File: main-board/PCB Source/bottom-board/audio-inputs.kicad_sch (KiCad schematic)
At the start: 86 parts, among them P10 JACK_TRS_6PINS, P9 JACK_TRS_6PINS, Q1 2N7002, Q2 2N7002, Q3 MMBFJ211, Q4 MMBFJ211, Q5 MMBFJ211, Q6 MMBFJ211, Q7 2N7002, Q8 2N7002, U14 LM833DR2G, U5 LM4562

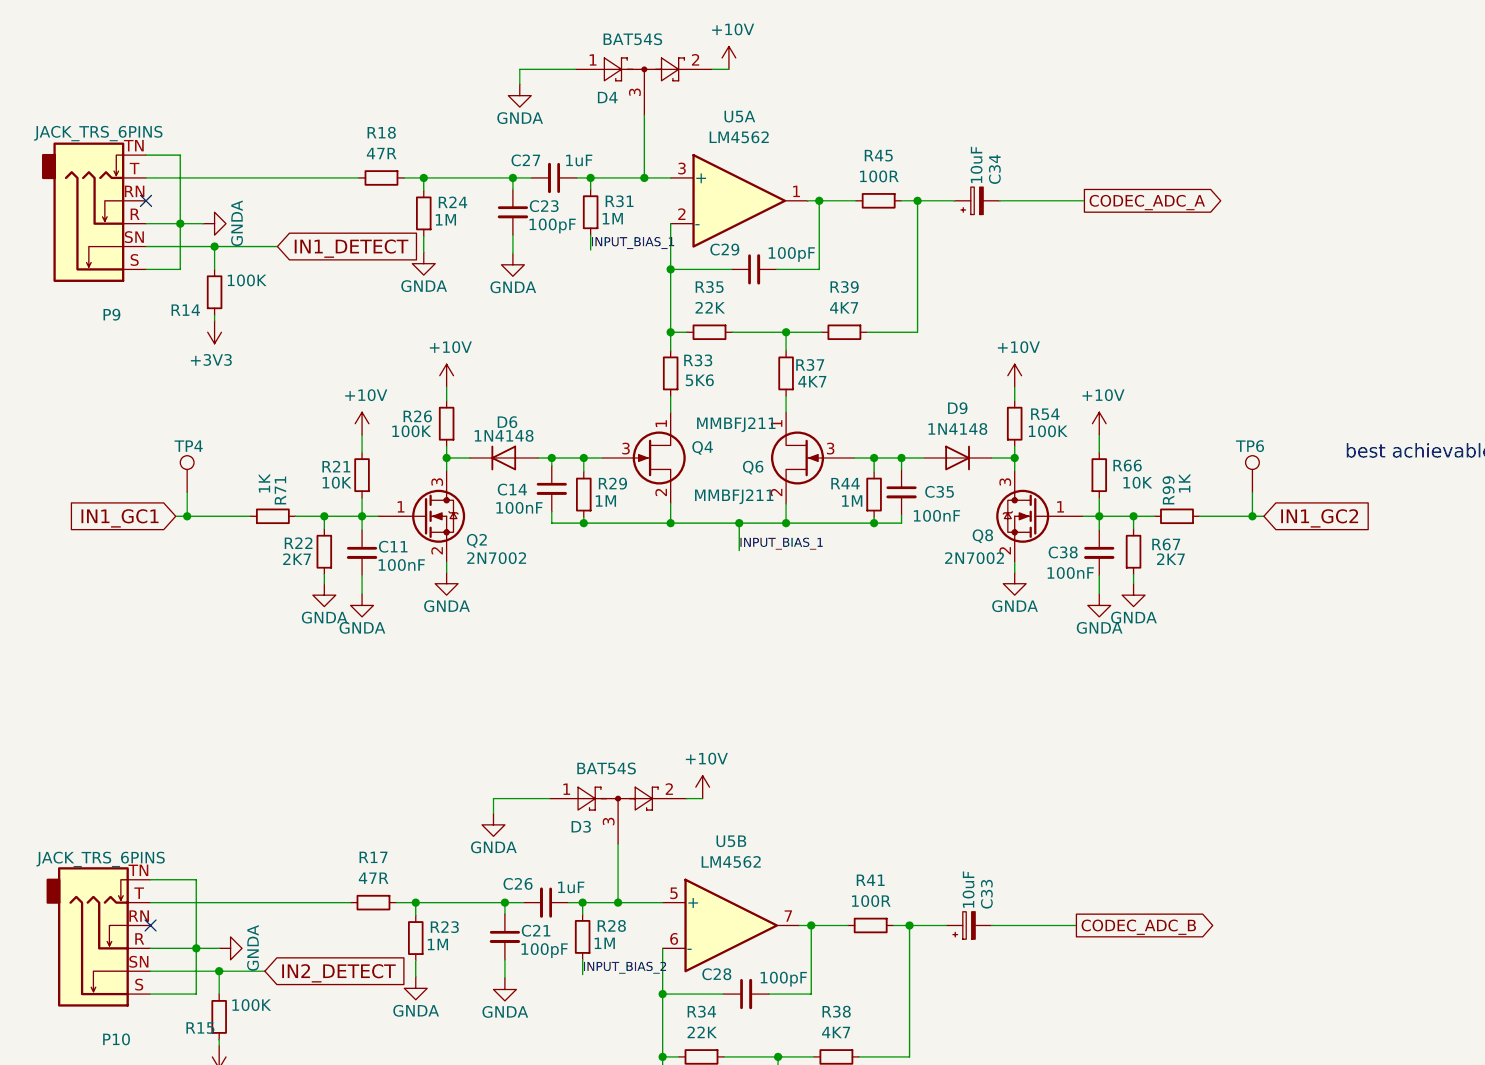
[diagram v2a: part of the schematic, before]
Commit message: icnrease diode footprint, add extra input cap option
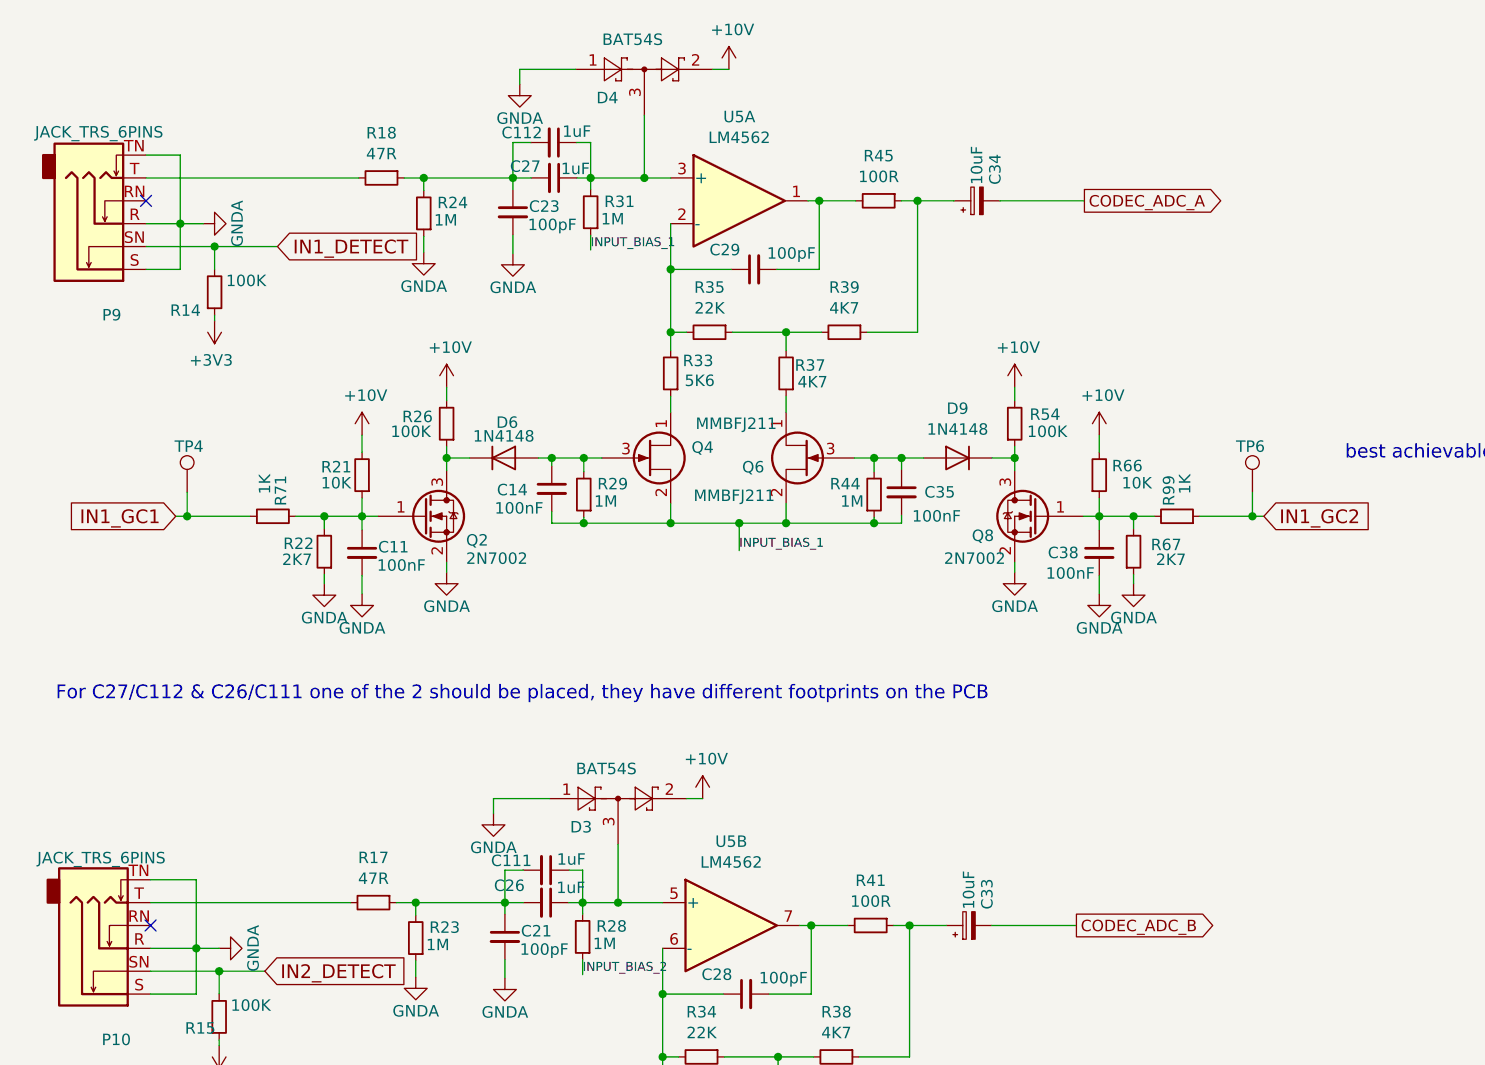
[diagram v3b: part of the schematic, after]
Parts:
- added C111, C112: 1uF, Capacitor_SMD:C_1210_3225Metric, symbol bottom-board-rescue:C_Small
- D5, D6, D8, D9: footprint Diode_SMD:D_SOD-323 -> Diode_SMD:D_SOD-323_HandSoldering
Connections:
- net at C23.1, C27.2, R18.1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: now also C112.2
- net at C27.1, D4.3, R31.2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: now also C112.1
- net at C26.1, D3.3, R28.2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: now also C111.1
- net at C21.1, C26.2, R17.1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: now also C111.2
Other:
- note added: "For C27/C112 & C26/C111 one of the 2 should be placed, they have different footprints on the PCB"
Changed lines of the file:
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@@
     (stroke (width 0) (type default) (color 0 0 0 0))
   )
+  (wire (pts (xy 82.931 26.416) (xy 82.931 30.353))
+    (stroke (width 0) (type default) (color 0 0 0 0))
+  )
   (wire (pts (xy 103.759 149.225) (xy 98.552 149.225))
     (stroke (width 0) (type default) (color 0 0 0 0))
@@
     (stroke (width 0) (type default) (color 0 0 0 0))
   )
-  (wire (pts (xy 64.389 30.353) (xy 74.295 30.353))
-    (stroke (width 0) (type default) (color 0 0 0 0))
-  )
   (wire (pts (xy 207.137 98.552) (xy 207.137 96.52))
     (stroke (width 0) (type default) (color 0 0 0 0))
@@
     (stroke (width 0) (type default) (color 0 0 0 0))
   )
+  (wire (pts (xy 73.406 107.2642) (xy 73.406 110.871))
+    (stroke (width 0) (type default) (color 0 0 0 0))
+  )
   (wire (pts (xy 117.475 67.818) (xy 117.475 68.707))
     (stroke (width 0) (type default) (color 0 0 0 0))
@@
     (stroke (width 0) (type default) (color 0 0 0 0))
   )
+  (wire (pts (xy 80.518 107.2642) (xy 82.042 107.2642))
+    (stroke (width 0) (type default) (color 0 0 0 0))
+  )
   (wire (pts (xy 231.648 155.321) (xy 232.918 155.321))
     (stroke (width 0) (type default) (color 0 0 0 0))
@@
     (stroke (width 0) (type default) (color 0 0 0 0))
   )
+  (wire (pts (xy 74.295 26.416) (xy 74.295 30.353))
+    (stroke (width 0) (type default) (color 0 0 0 0))
+  )
   (wire (pts (xy 117.475 61.468) (xy 119.888 61.468))
     (stroke (width 0) (type default) (color 0 0 0 0))
@@
     (stroke (width 0) (type default) (color 0 0 0 0))
   )
+  (wire (pts (xy 76.3016 26.416) (xy 74.295 26.416))
+    (stroke (width 0) (type default) (color 0 0 0 0))
+  )
   (wire (pts (xy 33.528 27.813) (xy 37.338 27.813))
     (stroke (width 0) (type default) (color 0 0 0 0))
@@
     (stroke (width 0) (type default) (color 0 0 0 0))
   )
+  (wire (pts (xy 82.042 107.2642) (xy 82.042 110.871))
+    (stroke (width 0) (type default) (color 0 0 0 0))
+  )
   (wire (pts (xy 102.743 121.031) (xy 107.442 121.031))
     (stroke (width 0) (type default) (color 0 0 0 0))
@@
     (stroke (width 0) (type default) (color 0 0 0 0))
   )
+  (wire (pts (xy 64.389 30.353) (xy 74.295 30.353))
+    (stroke (width 0) (type default) (color 0 0 0 0))
+  )
   (wire (pts (xy 111.379 141.986) (xy 113.538 141.986))
     (stroke (width 0) (type default) (color 0 0 0 0))
@@
     (stroke (width 0) (type default) (color 0 0 0 0))
   )
+  (wire (pts (xy 75.438 107.2642) (xy 73.406 107.2642))
+    (stroke (width 0) (type default) (color 0 0 0 0))
+  )
   (wire (pts (xy 129.413 140.716) (xy 129.413 141.986))
     (stroke (width 0) (type default) (color 0 0 0 0))
@@
     (stroke (width 0) (type default) (color 0 0 0 0))
   )
+  (wire (pts (xy 81.3816 26.416) (xy 82.931 26.416))
+    (stroke (width 0) (type default) (color 0 0 0 0))
+  )
   (wire (pts (xy 88.9 30.353) (xy 82.931 30.353))
     (stroke (width 0) (type default) (color 0 0 0 0))
@@
     (effects (font (size 1.524 1.524)) (justify left bottom))
   )
+  (text "For C27/C112 & C26/C111 one of the 2 should be placed, they have different footprints on the PCB"
+    (at 23.495 88.5952 0)
+    (effects (font (size 1.524 1.524)) (justify left bottom))
+  )
   (text "The gain calculation includes\nthe RDSon value\n\nJ110: RDSon = 18R"
     (at 218.821 40.767 0)
@@
   (symbol (lib_id "bottom-board-rescue:C_Small") (at 78.867 30.353 270) (unit 1)
     (in_bom yes) (on_board yes)
-    (property "Reference" "C27" (id 0) (at 74.041 28.448 90)
+    (property "Reference" "C27" (id 0) (at 73.9648 29.083 90)
       (effects (font (size 1.27 1.27)) (justify left))
     )
-    (property "Value" "1uF" (id 1) (at 80.01 28.448 90)
+    (property "Value" "1uF" (id 1) (at 79.629 29.337 90)
       (effects (font (size 1.27 1.27)) (justify left))
     )
@@
     (property "Reference" "D6" (id 0) (at 73.66 57.531 0))
     (property "Value" "1N4148" (id 1) (at 73.279 59.055 0))
-    (property "Footprint" "Diode_SMD:D_SOD-323" (id 2) (at 73.279 65.913 0)
+    (property "Footprint" "Diode_SMD:D_SOD-323_HandSoldering" (id 2) (at 73.279 65.913 0)
       (effects (font (size 1.27 1.27)) hide)
     )
@@
     (property "Reference" "D9" (id 0) (at 123.698 55.9816 0))
     (property "Value" "1N4148" (id 1) (at 123.698 58.293 0))
-    (property "Footprint" "Diode_SMD:D_SOD-323" (id 2) (at 123.698 65.913 0)
+    (property "Footprint" "Diode_SMD:D_SOD-323_HandSoldering" (id 2) (at 123.698 65.913 0)
       (effects (font (size 1.27 1.27)) hide)
     )
@@
   (symbol (lib_id "bottom-board-rescue:C_Small") (at 77.978 110.871 270) (unit 1)
     (in_bom yes) (on_board yes)
-    (property "Reference" "C26" (id 0) (at 73.152 108.839 90)
+    (property "Reference" "C26" (id 0) (at 72.1868 108.9914 90)
       (effects (font (size 1.27 1.27)) (justify left))
     )
@@
     (property "Reference" "D5" (id 0) (at 72.263 136.4996 0))
     (property "Value" "1N4148" (id 1) (at 72.263 138.811 0))
-    (property "Footprint" "Diode_SMD:D_SOD-323" (id 2) (at 72.263 146.431 0)
+    (property "Footprint" "Diode_SMD:D_SOD-323_HandSoldering" (id 2) (at 72.263 146.431 0)
       (effects (font (size 1.27 1.27)) hide)
     )
@@
     (property "Reference" "D8" (id 0) (at 123.063 136.4996 0))
     (property "Value" "1N4148" (id 1) (at 123.063 138.811 0))
-    (property "Footprint" "Diode_SMD:D_SOD-323" (id 2) (at 123.063 146.431 0)
+    (property "Footprint" "Diode_SMD:D_SOD-323_HandSoldering" (id 2) (at 123.063 146.431 0)
       (effects (font (size 1.27 1.27)) hide)
     )
@@
     (pin "1")
   )
+  (symbol (lib_id "bottom-board-rescue:C_Small") (at 77.978 107.2642 270) (unit 1)
+    (in_bom yes) (on_board yes)
+    (property "Reference" "C111" (id 0) (at 71.8566 106.2228 90)
+      (effects (font (size 1.27 1.27)) (justify left))
+    )
+    (property "Value" "1uF" (id 1) (at 79.1718 106.0704 90)
+      (effects (font (size 1.27 1.27)) (justify left))
+    )
+    (property "Footprint" "Capacitor_SMD:C_1210_3225Metric" (id 2) (at 77.978 107.2642 0)
+      (effects (font (size 1.524 1.524)) hide)
+    )
+    (property "Datasheet" "" (id 3) (at 77.978 107.2642 0)
+      (effects (font (size 1.524 1.524)))
+    )
+    (property "MPN" "FCA1210C105M-G2" (id 4) (at -57.912 -27.3558 0)
+      (effects (font (size 1.27 1.27)) hide)
+    )
+    (pin "1")
+    (pin "2")
+  )
   (symbol (lib_id "bottom-board-rescue:C_Small-Device") (at 197.358 146.812 0) (mirror y) (unit 1)
     (in_bom yes) (on_board yes)
@@
     (pin "1")
   )
+  (symbol (lib_id "bottom-board-rescue:C_Small") (at 78.8416 26.416 270) (unit 1)
+    (in_bom yes) (on_board yes)
+    (property "Reference" "C112" (id 0) (at 73.025 25.3492 90)
+      (effects (font (size 1.27 1.27)) (justify left))
+    )
+    (property "Value" "1uF" (id 1) (at 79.7814 25.1968 90)
+      (effects (font (size 1.27 1.27)) (justify left))
+    )
+    (property "Footprint" "Capacitor_SMD:C_1210_3225Metric" (id 2) (at 78.8416 26.416 0)
+      (effects (font (size 1.524 1.524)) hide)
+    )
+    (property "Datasheet" "" (id 3) (at 78.8416 26.416 0)
+      (effects (font (size 1.524 1.524)))
+    )
+    (property "MPN" "FCA1210C105M-G2" (id 4) (at -57.0484 -108.204 0)
+      (effects (font (size 1.27 1.27)) hide)
+    )
+    (pin "1")
+    (pin "2")
+  )
   (symbol (lib_id "bottom-board-rescue:LM4562-Amplifier_Operational") (at 208.28 147.32 0) (unit 3)
